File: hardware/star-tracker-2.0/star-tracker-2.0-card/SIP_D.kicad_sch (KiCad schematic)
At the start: 13 parts, among them J6 Conn_01x02, U7 OSD3358-512M-BSM

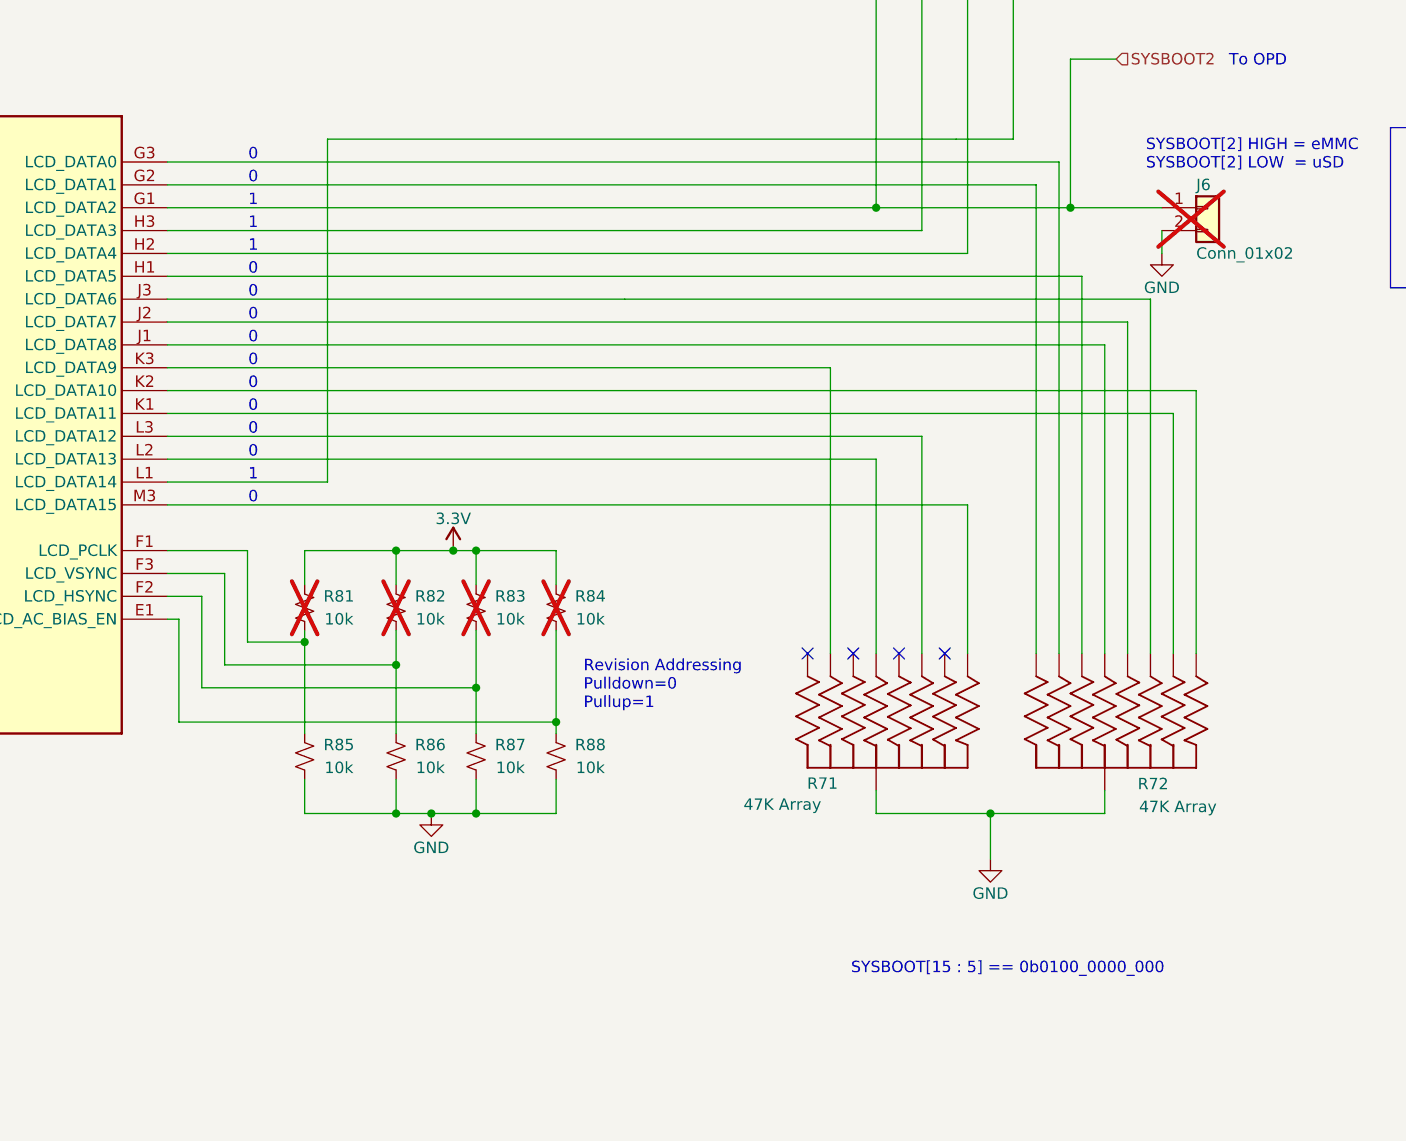
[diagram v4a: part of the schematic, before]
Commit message: Revert "Added pull up and pull down resistors"
This reverts commit cc5facaa3cbf2943c6d45776bf6d59f1c09cfd95.
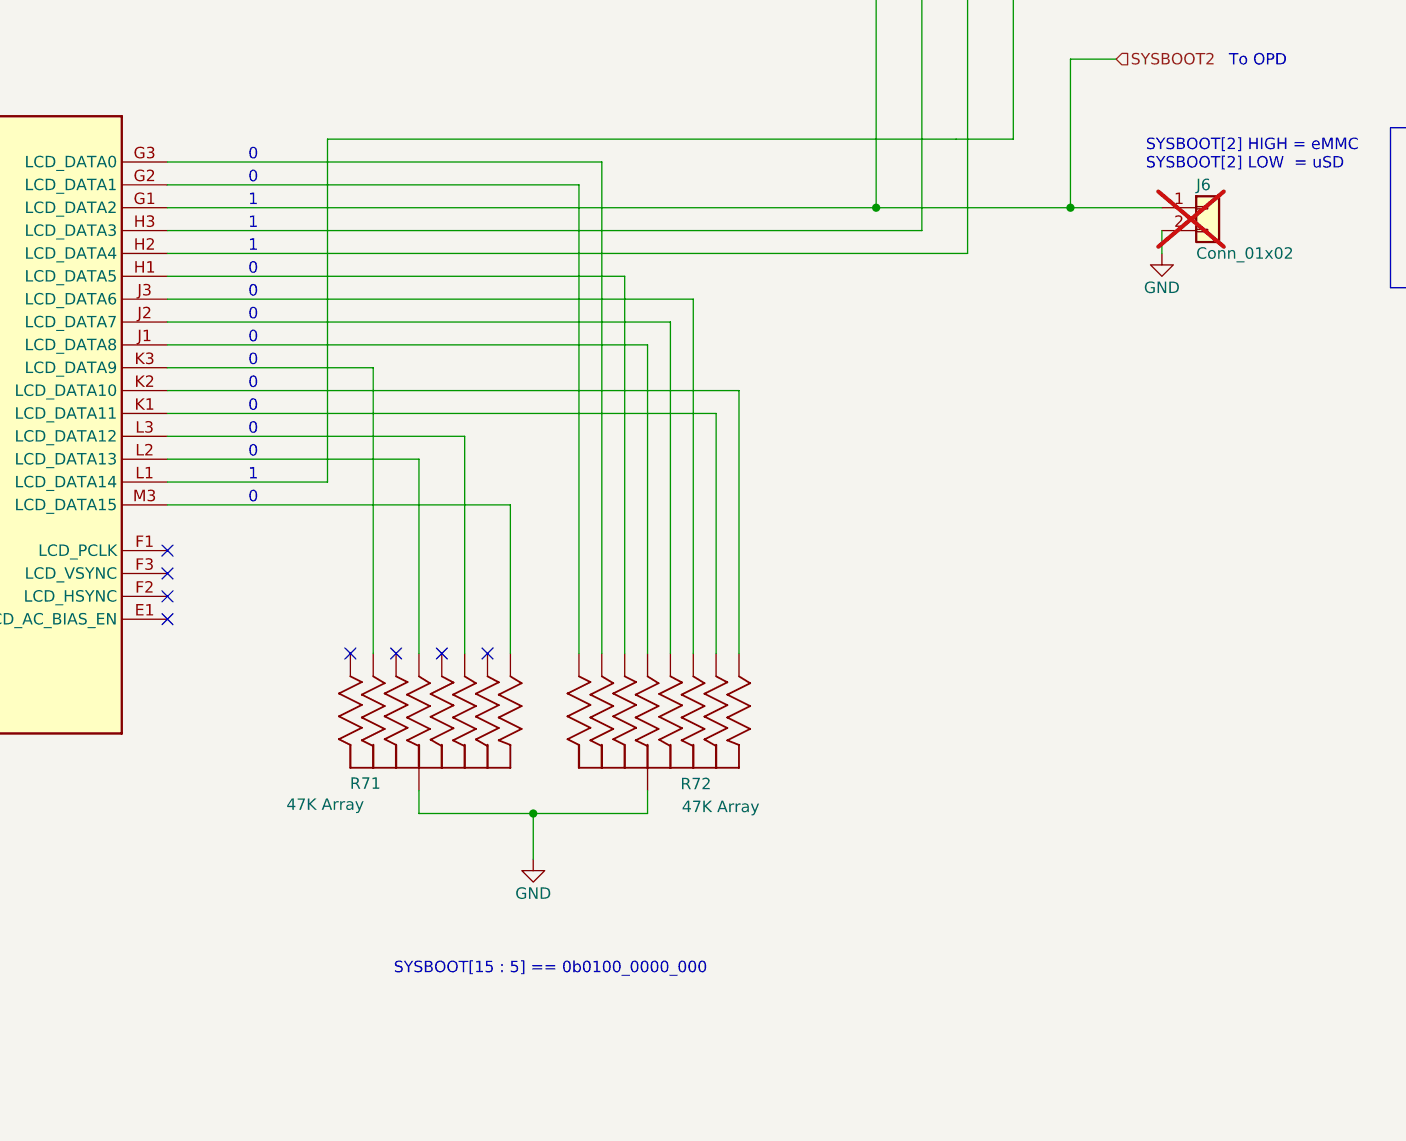
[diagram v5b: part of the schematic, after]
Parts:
- removed R81, R82, R83, R84, R85, R86, R87, R88: 10k, oresat-passives:0603-C-NOSILK, symbol Device:R_Small_US
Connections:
- no-connect marks 14 -> 18
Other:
- note removed: "Revision Addressing Pulldown=0 Pullup=1"
- moved on the sheet: R71, R72

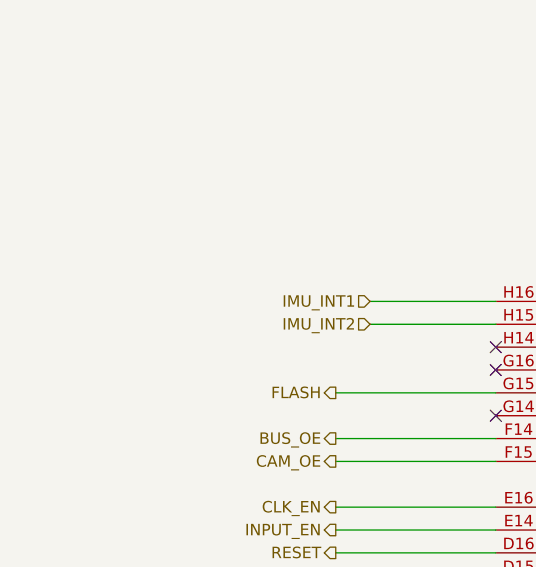
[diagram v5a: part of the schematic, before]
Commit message: Update
changed IMU to I2C bus 1, instead of shared bus 2 with the i2c camera control. Updated IMU interrupt pin location.
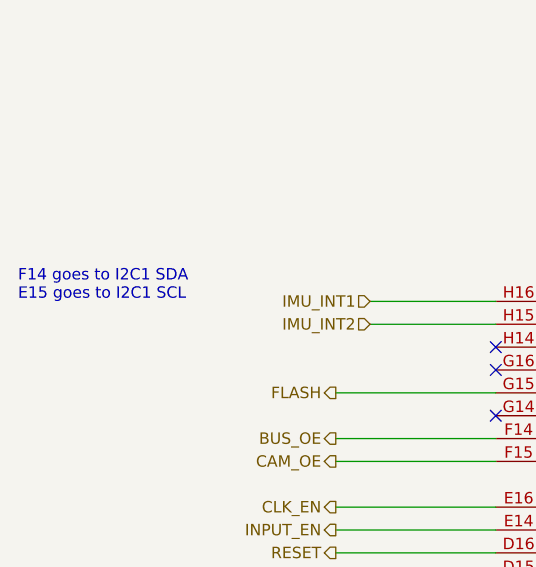
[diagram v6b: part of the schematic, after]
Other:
- note added: "E15 goes to I2C1 SCL"
- note added: "F14 goes to I2C1 SDA"
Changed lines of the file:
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@@
+		)
+	)
+	(text "F14 goes to I2C1 SDA"
+		(exclude_from_sim no)
+		(at 73.914 114.808 0)
+		(effects
+			(font
+				(size 1.27 1.27)
+			)
+			(justify left bottom)
 		)
 	)
@@
 		)
 	)
+	(text "E15 goes to I2C1 SCL"
+		(exclude_from_sim no)
+		(at 73.914 116.84 0)
+		(effects
+			(font
+				(size 1.27 1.27)
+			)
+			(justify left bottom)
+		)
+	)
